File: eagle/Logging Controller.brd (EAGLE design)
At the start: 98.7 x 48.2 mm, 59 parts, among them J1 PWR IN, U1 ATMEGA328P_PDIP, U2 LCD-1602 3V3, U3 MCP1700-3302E/TO, X1 32.768kHz, 6pF, X2 16MHz

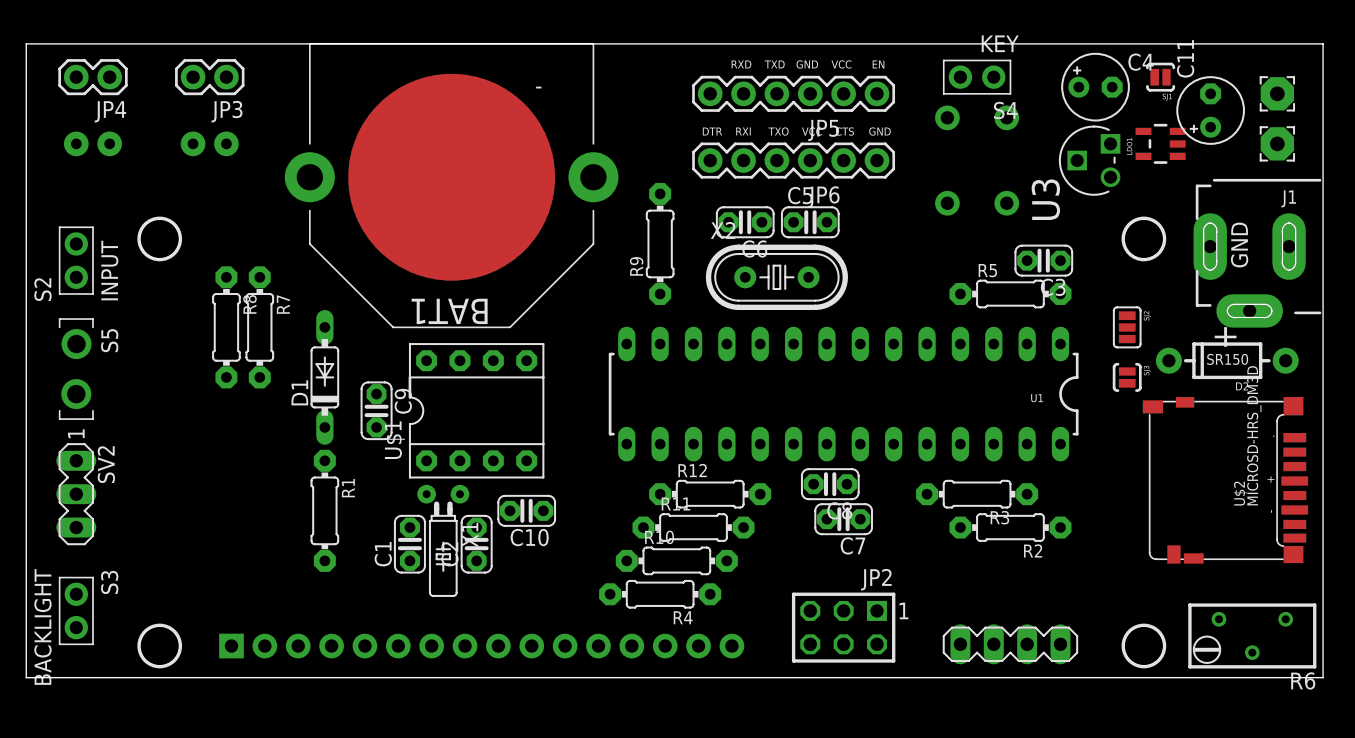
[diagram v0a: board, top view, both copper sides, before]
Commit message: tidied silk, adjusted some positions. Thick traces and ground fill
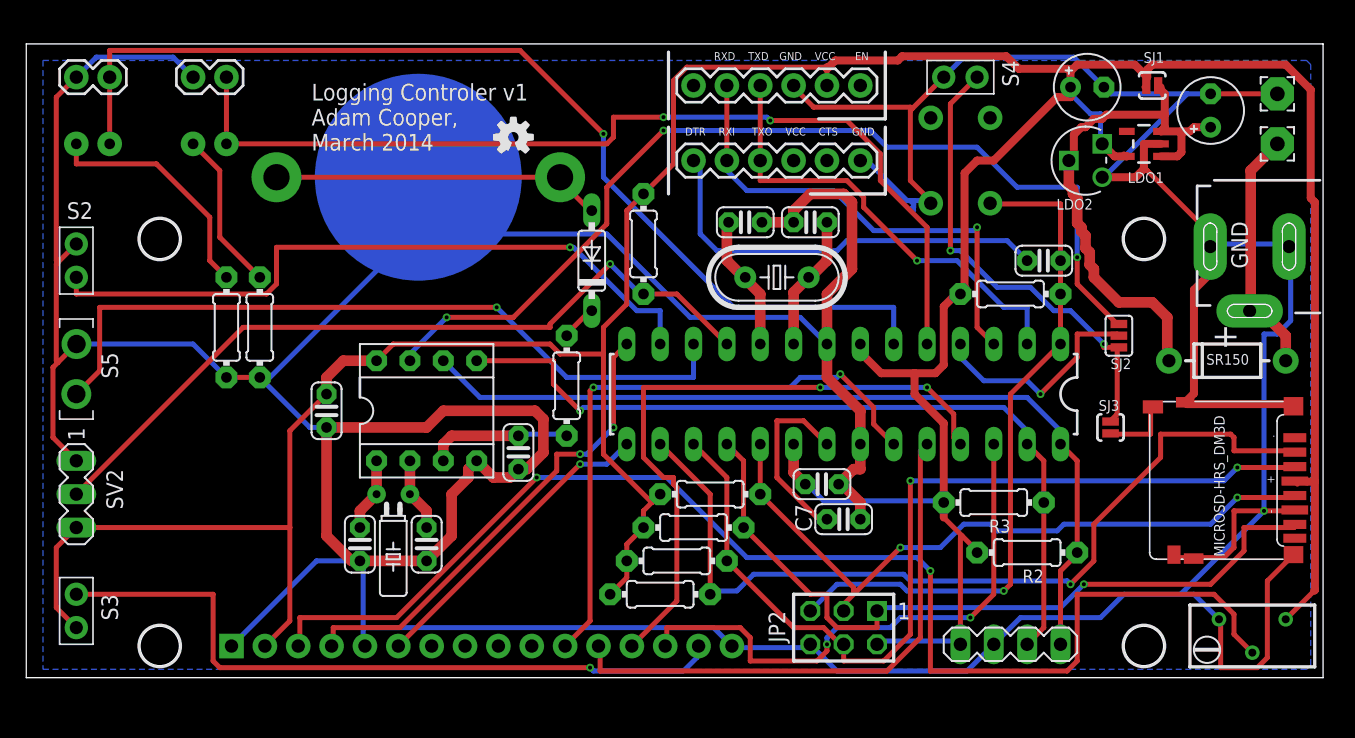
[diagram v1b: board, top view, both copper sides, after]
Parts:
- removed U3: MCP1700-3302E/TO, Logging Controller:TO127P254X495-3
- added LDO2: MCP1700-3302E/TO, Logging Controller:TO127P254X495-3
- SJ1: value Bypass LDO for 3V3 supp -> Bypass LDOs
- moved D1 22.2 mm to (43.1, 31.8)
- moved R1 20.7 mm to (41.1, 22.2)
- moved LOGO1 6.35 mm to (37.1, 41.1), flipped to the top
- moved C10 4.49 mm to (37.5, 17.1), turned to 90 degrees
- moved SJ3 4.02 mm to (82.5, 19.1)
- moved C1 3.81 mm to (25.4, 10.2)
- moved C9 3.81 mm to (22.9, 20.3)
- moved C2 3.81 mm to (30.5, 10.2)
- moved U$1 3.81 mm to (30.5, 20.3)
- moved X1 3.81 mm to (27.9, 14.0)
- moved BAT1 2.54 mm to (29.8, 38.1), flipped to the bottom
- moved R2 2.29 mm to (76.2, 9.53)
- moved JP5 1.42 mm to (50.8, 45.1)
- moved R3 1.42 mm to (73.7, 13.3)
- moved JP6 1.27 mm to (50.8, 39.4)
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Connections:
- net GND: now also LDO2.1; no longer U3.1
- net N$34: now also LDO2.2; no longer U3.2
- net VCC: now also LDO2.3; no longer U3.3
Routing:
- net GND: track 0.00 -> 469.9 mm, vias 0 -> 1
- net VCC: track 0.00 -> 304.8 mm
- net N$18: track 0.00 -> 97.8 mm, vias 0 -> 2
- net N$12: track 0.00 -> 79.6 mm, vias 0 -> 1
- net N$13: track 0.00 -> 73.7 mm, vias 0 -> 2
- net N$20: track 0.00 -> 73.6 mm, vias 0 -> 3
- net N$22: track 0.00 -> 70.2 mm, vias 0 -> 2
- net N$2: track 0.00 -> 67.1 mm, vias 0 -> 1
- net N$28: track 0.00 -> 66.5 mm
- net N$27: track 0.00 -> 62.7 mm, vias 0 -> 1
- net N$1: track 0.00 -> 59.5 mm, vias 0 -> 1
- net N$23: track 0.00 -> 58.2 mm, vias 0 -> 1
- net N$11: track 0.00 -> 57.3 mm, vias 0 -> 1
- net N$9: track 0.00 -> 54.0 mm, vias 0 -> 1
- net N$10: track 0.00 -> 53.4 mm, vias 0 -> 1
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- added copper zone on layer 16, net GND
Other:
- board text added: "1 - VSS"

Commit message: v1.0.1 revision, esp fix power in pinout.
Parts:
- C4: value 10u -> 100u
- moved D2 1.27 mm to (90.2, 24.1)
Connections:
- net GND: now also J1.GND, J1.GND2; no longer J1.CONTACT, J1.OUTER-GND
- net N$36: now also J1.POS; no longer J1.CENTRE-POS
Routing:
- net GND: track 469.9 -> 431.5 mm
- net N$36: track 19.0 -> 24.6 mm
- net N$34: track 41.1 -> 39.7 mm
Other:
- board text added: "+ve"
- board text added: "GND"
- board text added: "Logging Controler v1.0.1 Adam Cooper, March 2014"
- board text added: "SCL"
- board text added: "SDA"
- board text added: "a"
- board text removed: "Logging Controler v1 Adam Cooper, March 2014"
